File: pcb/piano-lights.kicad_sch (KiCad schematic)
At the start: 39 parts, among them J1 USB-C 6-Pin, J2 FTDI RS232, J3 LED Strip, J4 AVR-ISP-6, J5 MIDI IN, J6 MIDI THRU, J7 MIDI Coupler B, J8 MIDI Coupler A, SW1 Button, SW2 Reset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

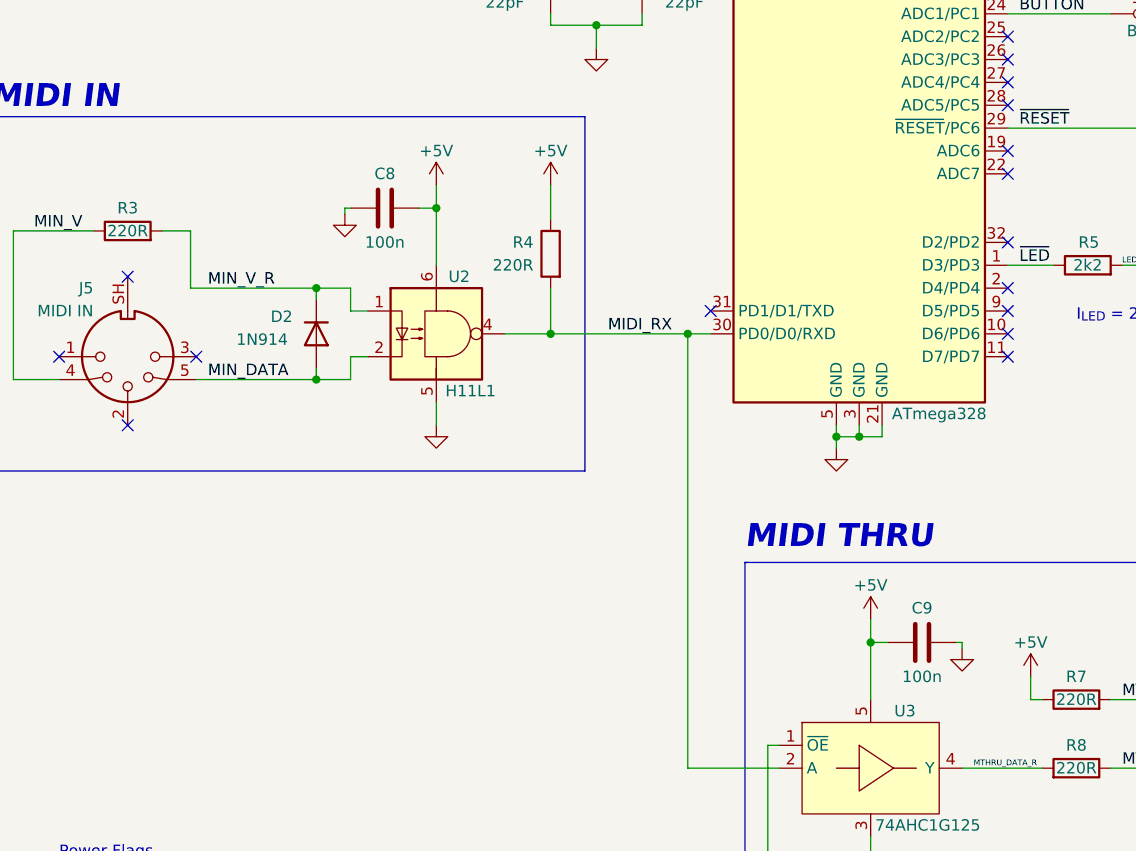
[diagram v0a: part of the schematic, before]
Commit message: Fix new ERC errors (mostly grid issues, with some symbol updates)
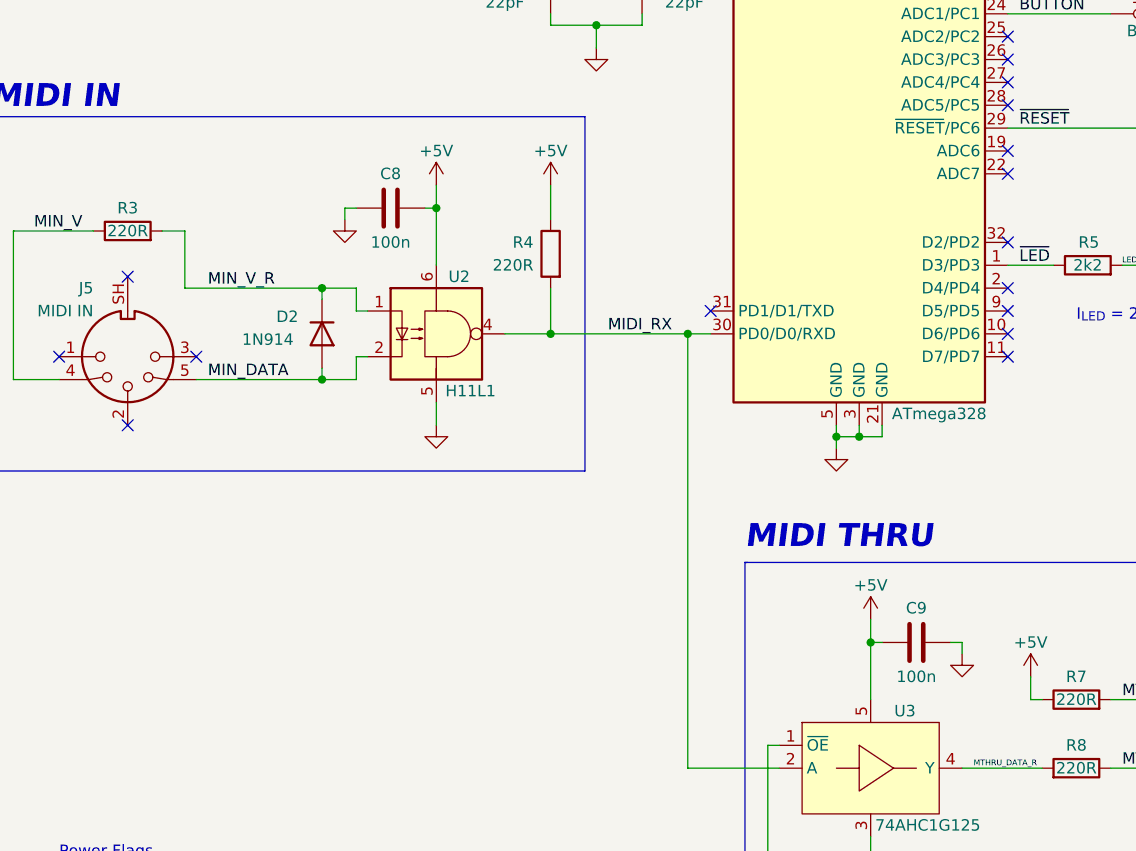
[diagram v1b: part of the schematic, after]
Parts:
- D2: footprint Diode_SMD:D_SOD-123 -> Diode_THT:D_DO-35_SOD27_P7.62mm_Horizontal
- J2: symbol Connector:Conn_01x06_Male -> Connector:Conn_01x06_Pin
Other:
- moved on the sheet: C8, C9, D2

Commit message: Switch to 0603 package for LED #7
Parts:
- D1: footprint LED_SMD:LED_0805_2012Metric_Pad1.15x1.40mm_HandSolder -> LED_SMD:LED_0603_1608Metric_Pad1.05x0.95mm_HandSolder; Mfr Lumex -> Rohm; Mfr Part SML-LXT0805IW-TR -> SML-D12U8WT86; Vendor https://www.digikey.com/short/pq7bjprd -> https://www.digikey.com/short/h5q7qdm2
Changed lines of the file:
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@@
       (effects (font (size 1.27 1.27)))
     )
-    (property "Footprint" "LED_SMD:LED_0805_2012Metric_Pad1.15x1.40mm_HandSolder" (at 151.13 93.98 0)
+    (property "Footprint" "LED_SMD:LED_0603_1608Metric_Pad1.05x0.95mm_HandSolder" (at 151.13 93.98 0)
       (effects (font (size 1.27 1.27)) hide)
     )
@@
       (effects (font (size 1.27 1.27)) hide)
     )
-    (property "Mfr" "Lumex" (at 151.13 93.98 0)
+    (property "Mfr" "Rohm" (at 151.13 93.98 0)
       (effects (font (size 1.27 1.27)) hide)
     )
-    (property "Mfr Part" "SML-LXT0805IW-TR" (at 151.13 93.98 0)
+    (property "Mfr Part" "SML-D12U8WT86" (at 151.13 93.98 0)
       (effects (font (size 1.27 1.27)) hide)
     )
-    (property "Vendor" "https://www.digikey.com/short/pq7bjprd" (at 151.13 93.98 0)
+    (property "Vendor" "https://www.digikey.com/short/h5q7qdm2" (at 151.13 93.98 0)
       (effects (font (size 1.27 1.27)) hide)
     )

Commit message: Fix up diode footprint
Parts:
- D2: footprint Diode_THT:D_DO-35_SOD27_P7.62mm_Horizontal -> Diode_SMD:D_SOD-123
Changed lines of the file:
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@@
       (effects (font (size 1.27 1.27)) (justify left))
     )
-    (property "Footprint" "Diode_THT:D_DO-35_SOD27_P7.62mm_Horizontal" (at 50.165 101.6 0)
+    (property "Footprint" "Diode_SMD:D_SOD-123" (at 50.165 101.6 0)
       (effects (font (size 1.27 1.27)) hide)
     )

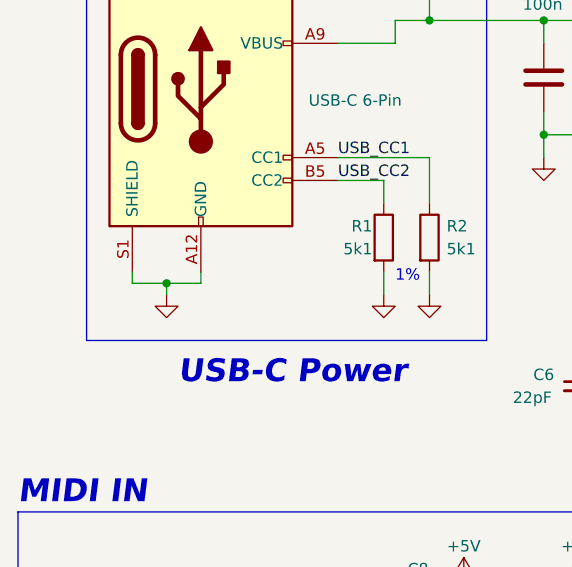
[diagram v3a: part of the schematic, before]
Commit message: Tie USB-C shield to earth and add a 4n7F cap between earth and ground
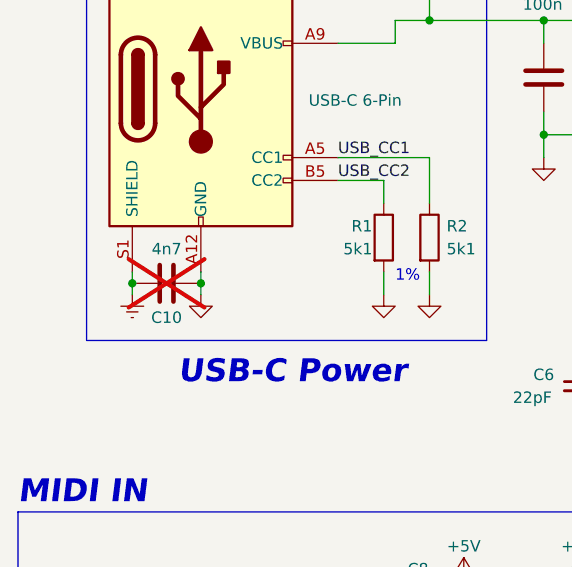
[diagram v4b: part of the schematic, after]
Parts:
- added C10: 4n7, Capacitor_SMD:C_0603_1608Metric_Pad1.08x0.95mm_HandSolder, symbol Device:C
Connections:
- net GND: now also C10.1; no longer J1.S1 (SHIELD)
- new net Earth: C10.2, J1.S1 (SHIELD)
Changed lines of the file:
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@@
   (junction (at 175.26 67.31) (diameter 0) (color 0 0 0 0)
   )
+  (junction (at 38.1 52.07) (diameter 0) (color 0 0 0 0)
+  )
   (junction (at 115.57 34.29) (diameter 0) (color 0 0 0 0)
   )
@@
   (junction (at 76.2 35.56) (diameter 0) (color 0 0 0 0)
   )
-  (junction (at 34.29 52.07) (diameter 0) (color 0 0 0 0)
-  )
   (junction (at 111.76 113.03) (diameter 0) (color 0 0 0 0)
   )
@@
   )
   (junction (at 95.25 101.6) (diameter 0) (color 0 0 0 0)
+  )
+  (junction (at 30.48 52.07) (diameter 0) (color 0 0 0 0)
   )
   (junction (at 85.09 67.31) (diameter 0) (color 0 0 0 0)
@@
     (stroke (width 0) (type default))
   )
-  (wire (pts (xy 34.29 52.07) (xy 34.29 53.34))
-    (stroke (width 0) (type default))
-  )
   (wire (pts (xy 133.35 139.7) (xy 133.35 142.24))
     (stroke (width 0) (type default))
@@
     (stroke (width 0) (type default))
   )
-  (wire (pts (xy 30.48 52.07) (xy 34.29 52.07))
-    (stroke (width 0) (type default))
-  )
   (wire (pts (xy 165.1 91.44) (xy 165.1 92.71))
     (stroke (width 0) (type default))
@@
     (stroke (width 0) (type default))
   )
+  (wire (pts (xy 30.48 52.07) (xy 30.48 53.34))
+    (stroke (width 0) (type default))
+  )
   (wire (pts (xy 223.52 133.35) (xy 233.68 133.35))
     (stroke (width 0) (type default))
@@
     (stroke (width 0) (type default))
   )
+  (wire (pts (xy 38.1 52.07) (xy 38.1 53.34))
+    (stroke (width 0) (type default))
+  )
   (polyline (pts (xy 101.6 127) (xy 177.8 127))
     (stroke (width 0) (type default))
@@
   )
   (wire (pts (xy 130.81 43.18) (xy 181.61 43.18))
-    (stroke (width 0) (type default))
-  )
-  (wire (pts (xy 34.29 52.07) (xy 38.1 52.07))
     (stroke (width 0) (type default))
   )
@@
         (path "/b6aa007d-aa4c-4e78-ae8f-c5ed1bbb4e88"
           (reference "C2") (unit 1)
+        )
+      )
+    )
+  )
+  (symbol (lib_id "power:Earth") (at 30.48 53.34 0) (unit 1)
+    (in_bom yes) (on_board yes) (dnp no) (fields_autoplaced)
+    (property "Reference" "#PWR033" (at 30.48 59.69 0)
+      (effects (font (size 1.27 1.27)) hide)
+    )
+    (property "Value" "Earth" (at 30.48 57.15 0)
+      (effects (font (size 1.27 1.27)) hide)
+    )
+    (property "Footprint" "" (at 30.48 53.34 0)
+      (effects (font (size 1.27 1.27)) hide)
+    )
+    (property "Datasheet" "~" (at 30.48 53.34 0)
+      (effects (font (size 1.27 1.27)) hide)
+    )
+    (pin "1")
+    (instances
+      (project "piano-lights"
+        (path "/b6aa007d-aa4c-4e78-ae8f-c5ed1bbb4e88"
+          (reference "#PWR033") (unit 1)
         )
       )
@@
     )
   )
+  (symbol (lib_id "Device:C") (at 34.29 52.07 270) (unit 1)
+    (in_bom yes) (on_board yes) (dnp yes)
+    (property "Reference" "C10" (at 34.29 55.88 90)
+      (effects (font (size 1.27 1.27)))
+    )
+    (property "Value" "4n7" (at 34.29 48.26 90)
+      (effects (font (size 1.27 1.27)))
+    )
+    (property "Footprint" "Capacitor_SMD:C_0603_1608Metric_Pad1.08x0.95mm_HandSolder" (at 30.48 53.0352 0)
+      (effects (font (size 1.27 1.27)) hide)
+    )
+    (property "Datasheet" "~" (at 34.29 52.07 0)
+      (effects (font (size 1.27 1.27)) hide)
+    )
+    (property "Mfr" "" (at 34.29 52.07 0)
+      (effects (font (size 1.27 1.27)) hide)
+    )
+    (property "Mfr Part" "" (at 34.29 52.07 0)
+      (effects (font (size 1.27 1.27)) hide)
+    )
+    (property "Vendor" "" (at 34.29 52.07 0)
+      (effects (font (size 1.27 1.27)) hide)
+    )
+    (pin "1")
+    (pin "2")
+    (instances
+      (project "piano-lights"
+        (path "/b6aa007d-aa4c-4e78-ae8f-c5ed1bbb4e88"
+          (reference "C10") (unit 1)
+        )
+      )
+    )
+  )
   (symbol (lib_id "power:+5V") (at 165.1 29.21 0) (mirror y) (unit 1)
     (in_bom yes) (on_board yes) (dnp no)
@@
     )
   )
-  (symbol (lib_id "power:GND") (at 34.29 53.34 0) (unit 1)
+  (symbol (lib_id "power:GND") (at 38.1 53.34 0) (unit 1)
     (in_bom yes) (on_board yes) (dnp no) (fields_autoplaced)
-    (property "Reference" "#PWR06" (at 34.29 59.69 0)
-      (effects (font (size 1.27 1.27)) hide)
-    )
-    (property "Value" "GND" (at 34.29 58.42 0)
-      (effects (font (size 1.27 1.27)) hide)
-    )
-    (property "Footprint" "" (at 34.29 53.34 0)
-      (effects (font (size 1.27 1.27)) hide)
-    )
-    (property "Datasheet" "" (at 34.29 53.34 0)
-      (effects (font (size 1.27 1.27)) hide)
-    )
+    (property "Reference" "#PWR06" (at 38.1 59.69 0)
+      (effects (font (size 1.27 1.27)) hide)
+    )
+    (property "Value" "GND" (at 38.1 58.42 0)
+      (effects (font (size 1.27 1.27)) hide)
+    )
+    (property "Footprint" "" (at 38.1 53.34 0)
+      (effects (font (size 1.27 1.27)) hide)
+    )
+    (property "Datasheet" "" (at 38.1 53.34 0)
+      (effects (font (size 1.27 1.27)) hide)
+    )

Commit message: Switch Earth to GND capacitor to 0803 (from 0603)
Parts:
- C10: footprint Capacitor_SMD:C_0603_1608Metric_Pad1.08x0.95mm_HandSolder -> Capacitor_SMD:C_0805_2012Metric_Pad1.18x1.45mm_HandSolder; Mfr (none) -> Murata; Mfr Part (none) -> GRM2165C1H472JA01D; Vendor (none) -> https://www.digikey.com/short/rpdfwwfw
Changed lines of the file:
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@@
       (effects (font (size 1.27 1.27)))
     )
-    (property "Footprint" "Capacitor_SMD:C_0603_1608Metric_Pad1.08x0.95mm_HandSolder" (at 30.48 53.0352 0)
+    (property "Footprint" "Capacitor_SMD:C_0805_2012Metric_Pad1.18x1.45mm_HandSolder" (at 30.48 53.0352 0)
       (effects (font (size 1.27 1.27)) hide)
     )
@@
       (effects (font (size 1.27 1.27)) hide)
     )
-    (property "Mfr" "" (at 34.29 52.07 0)
+    (property "Mfr" "Murata" (at 34.29 52.07 0)
       (effects (font (size 1.27 1.27)) hide)
     )
-    (property "Mfr Part" "" (at 34.29 52.07 0)
+    (property "Mfr Part" "GRM2165C1H472JA01D" (at 34.29 52.07 0)
       (effects (font (size 1.27 1.27)) hide)
     )
-    (property "Vendor" "" (at 34.29 52.07 0)
+    (property "Vendor" "https://www.digikey.com/short/rpdfwwfw" (at 34.29 52.07 0)
       (effects (font (size 1.27 1.27)) hide)
     )

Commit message: Update all versions to 3.0.0 and update date
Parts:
- C10: now fitted
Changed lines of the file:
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@@
   (title_block
     (title "Piano Lights")
-    (date "2023-02-22")
-    (rev "2.0.0")
+    (date "2023-07-04")
+    (rev "3.0.0")
     (company "Dave Dribin")
   )
@@
   )
   (symbol (lib_id "Device:C") (at 34.29 52.07 270) (unit 1)
-    (in_bom yes) (on_board yes) (dnp yes)
+    (in_bom yes) (on_board yes) (dnp no)
     (property "Reference" "C10" (at 34.29 55.88 90)
       (effects (font (size 1.27 1.27)))

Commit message: Update CHANGELOG and update release date
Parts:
- U1: value ATmega328 -> ATmega328(P)
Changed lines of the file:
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@@
   (title_block
     (title "Piano Lights")
-    (date "2023-07-04")
+    (date "2023-07-05")
     (rev "3.0.0")
     (company "Dave Dribin")
@@
       (effects (font (size 1.27 1.27)))
     )
-    (property "Value" "ATmega328" (at 123.19 110.49 0)
+    (property "Value" "ATmega328(P)" (at 123.19 110.49 0)
       (effects (font (size 1.27 1.27)))
     )

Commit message: Add text about JST XH connector on schematic
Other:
- note added: "JST XH Connector"
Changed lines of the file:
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@@
     (effects (font (size 1.27 1.27)) (justify left bottom))
+  )
+  (text "JST XH Connector" (at 228.6 51.435 0)
+    (effects (font (face "Menlo") (size 1.27 1.27)) (justify left bottom))
   )
   (text "I_{LED} = 2.3mA" (at 138.43 100.33 0)
